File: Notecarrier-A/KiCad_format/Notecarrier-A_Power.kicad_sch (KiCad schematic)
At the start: 42 parts, among them J10 00711, J12 B2B-PH-SM4-TBT(LF)(SN), J19 10118192-0002LF, J19 NU, J3 B2B-PH-SM4-TBT(LF)(SN), J4 B2B-PH-SM4-TBT(LF)(SN), J9 12734, SW1 CJS-1200TA, U2 BQ24210DQCT, U3 MAX17225ELT, U4 TPS62748YFPT

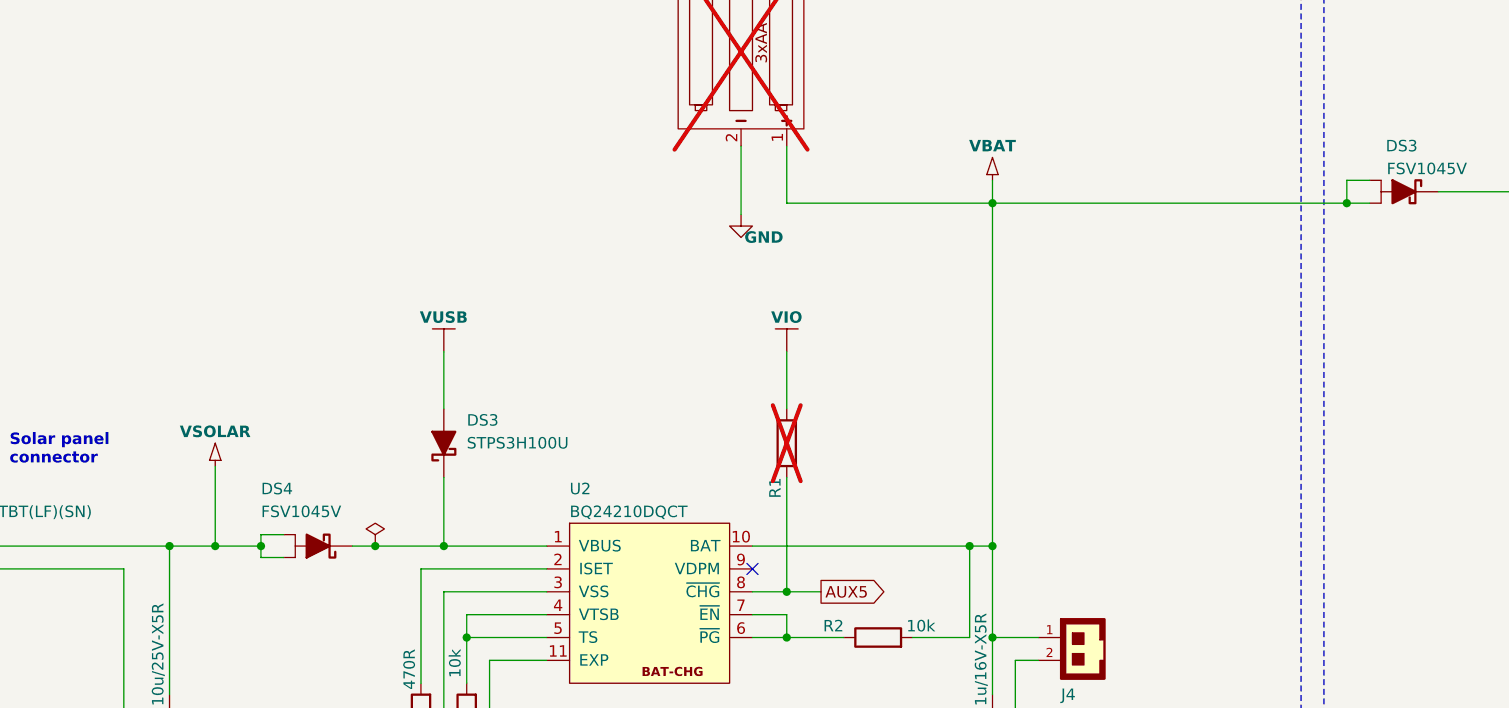
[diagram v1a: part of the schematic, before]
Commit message: First pass port of Notecarrier-B PCB.
See PortingNotes for details. To go: 3D models and validation.
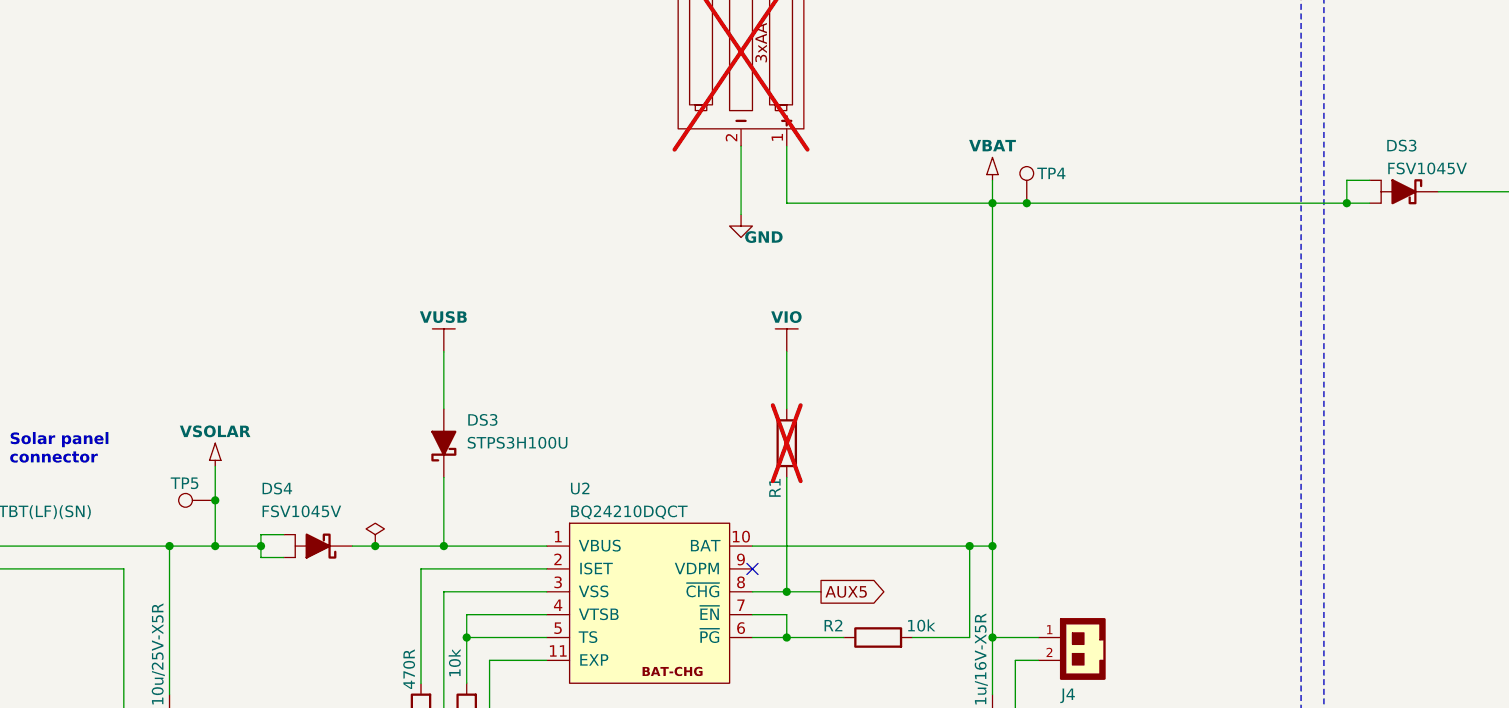
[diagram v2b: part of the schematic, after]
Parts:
- added TP4, TP5: TPS, blues-kicad-lib:TPS-SPEA, symbol Connector:TestPoint
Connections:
- net VBAT: now also TP4.1
- net VSOLAR: now also TP5.1
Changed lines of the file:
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@@
   (junction (at 298.45 205.74) (diameter 0) (color 0 0 0 0)
   )
+  (junction (at 55.88 153.67) (diameter 0) (color 0 0 0 0)
+  )
   (junction (at 293.37 121.92) (diameter 0) (color 0 0 0 0)
   )
@@
   (junction (at 50.8 158.75) (diameter 0) (color 0 0 0 0)
   )
+  (junction (at 146.05 120.65) (diameter 0) (color 0 0 0 0)
+  )
   (junction (at 55.88 158.75) (diameter 0) (color 0 0 0 0)
   )
@@
     (stroke (width 0.6) (type default) (color 0 0 0 1))
   )
+  (wire (pts (xy 50.8 158.75) (xy 55.88 158.75))
+    (stroke (width 0) (type default))
+  )
   (wire (pts (xy 246.38 101.6) (xy 290.83 101.6))
     (stroke (width 0.6) (type default) (color 132 132 132 1))
@@
     (stroke (width 0) (type default))
   )
-  (wire (pts (xy 55.88 158.75) (xy 50.8 158.75))
-    (stroke (width 0) (type default))
-  )
   (wire (pts (xy 290.83 152.4) (xy 290.83 127))
     (stroke (width 0.6) (type default) (color 0 0 0 1))
@@
     (stroke (width 0) (type default))
   )
-  (wire (pts (xy 142.24 120.65) (xy 181.61 120.65))
+  (wire (pts (xy 142.24 120.65) (xy 146.05 120.65))
     (stroke (width 0.6) (type default) (color 255 128 0 1))
   )
@@
     (stroke (width 0.6) (type default) (color 132 132 132 1))
   )
+  (wire (pts (xy 55.88 153.67) (xy 55.88 158.75))
+    (stroke (width 0) (type default))
+  )
   (wire (pts (xy 382.27 121.92) (xy 382.27 139.7))
     (stroke (width 0.6) (type default) (color 255 0 255 1))
@@
     (stroke (width 0) (type default))
   )
-  (wire (pts (xy 55.88 149.86) (xy 55.88 158.75))
+  (wire (pts (xy 55.88 149.86) (xy 55.88 153.67))
     (stroke (width 0) (type default))
   )
@@
     (stroke (width 0) (type default))
   )
+  (wire (pts (xy 146.05 120.65) (xy 181.61 120.65))
+    (stroke (width 0.6) (type default) (color 255 128 0 1))
+  )
   (wire (pts (xy 293.37 121.92) (xy 298.45 121.92))
     (stroke (width 0) (type default))
@@
     )
   )
+  (symbol (lib_id "Connector:TestPoint") (at 146.05 120.65 0) (unit 1)
+    (in_bom yes) (on_board yes) (dnp no)
+    (property "Reference" "TP4" (at 147.2208 117.3891 0)
+      (effects (font (size 1.27 1.27)) (justify left))
+    )
+    (property "Value" "TPS" (at 147.32 119.38 0)
+      (effects (font (size 1.27 1.27)) (justify left) hide)
+    )
+    (property "Footprint" "blues-kicad-lib:TPS-SPEA" (at 151.13 120.65 0)
+      (effects (font (size 1.27 1.27)) hide)
+    )
+    (property "Datasheet" "~" (at 151.13 120.65 0)
+      (effects (font (size 1.27 1.27)) hide)
+    )
+    (property "Critical" "" (at 146.05 120.65 0)
+      (effects (font (size 1.27 1.27)) hide)
+    )
+    (property "Description" "" (at 146.05 120.65 0)
+      (effects (font (size 1.27 1.27)) hide)
+    )
+    (property "Manufacturer" "" (at 146.05 120.65 0)
+      (effects (font (size 1.27 1.27)) hide)
+    )
+    (property "Order Code" "" (at 146.05 120.65 0)
+      (effects (font (size 1.27 1.27)) hide)
+    )
+    (property "Part Number" "" (at 146.05 120.65 0)
+      (effects (font (size 1.27 1.27)) hide)
+    )
+    (property "Supplier" "" (at 146.05 120.65 0)
+      (effects (font (size 1.27 1.27)) hide)
+    )
+    (pin "1")
+    (instances
+      (project "Notecarrier-A"
+        (path "/5050c972-9893-4dc9-ac8b-afa1eb9e3ab8/03718417-b36a-4e5d-916f-df242c9477be"
+          (reference "TP4") (unit 1)
+        )
+      )
+    )
+  )
   (symbol (lib_id "Connector_Generic:Conn_01x03") (at 292.1 205.74 0) (mirror y) (unit 1)
     (in_bom yes) (on_board yes) (dnp no)
@@
         )
       )
+    )
+  )
+  (symbol (lib_id "Connector:TestPoint") (at 55.88 153.67 90) (unit 1)
+    (in_bom yes) (on_board yes) (dnp no)
+    (property "Reference" "TP5" (at 54.1541 151.8113 90)
+      (effects (font (size 1.27 1.27)) (justify left))
+    )
+    (property "Value" "TPS" (at 53.34 156.21 90)
+      (effects (font (size 1.27 1.27)) (justify left) hide)
+    )
+    (property "Footprint" "blues-kicad-lib:TPS-SPEA" (at 55.88 148.59 0)
+      (effects (font (size 1.27 1.27)) hide)
+    )
+    (property "Datasheet" "~" (at 55.88 148.59 0)
+      (effects (font (size 1.27 1.27)) hide)
+    )
+    (property "Critical" "" (at 55.88 153.67 0)
+      (effects (font (size 1.27 1.27)) hide)
+    )
+    (property "Description" "" (at 55.88 153.67 0)
+      (effects (font (size 1.27 1.27)) hide)
+    )
+    (property "Manufacturer" "" (at 55.88 153.67 0)
+      (effects (font (size 1.27 1.27)) hide)
+    )
+    (property "Order Code" "" (at 55.88 153.67 0)
+      (effects (font (size 1.27 1.27)) hide)
+    )
+    (property "Part Number" "" (at 55.88 153.67 0)
+      (effects (font (size 1.27 1.27)) hide)
+    )
+    (property "Supplier" "" (at 55.88 153.67 0)
+      (effects (font (size 1.27 1.27)) hide)
+    )
+    (pin "1")
+    (instances
+      (project "Notecarrier-A"
+        (path "/5050c972-9893-4dc9-ac8b-afa1eb9e3ab8/03718417-b36a-4e5d-916f-df242c9477be"
+          (reference "TP5") (unit 1)
+        )
+      )

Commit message: Release RevA of Notecarrier-A port.
Validation complete. Results in the validation directory, documented in PortingNotes.md.
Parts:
- R1: value 10k -> NU
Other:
- note added: "Additional Interfaces"
- moved on the sheet: C1, J10, J12, J3, PAD1, PAD2, TP5

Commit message: Back port J-5-0065-FOS-USB10118192-NOF footprint from Notecarrier-Pi.
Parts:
- J19: footprint blues-kicad-lib:J-5-0065-FOS-MICROUSB10118192 -> blues-kicad-lib:J-5-0065-FOS-USB10118192-NOF
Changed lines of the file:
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@@
       (effects (font (size 1.27 1.27)) (justify left) hide)
     )
-    (property "Footprint" "blues-kicad-lib:J-5-0065-FOS-MICROUSB10118192" (at 128.27 260.35 0)
+    (property "Footprint" "blues-kicad-lib:J-5-0065-FOS-USB10118192-NOF" (at 128.27 260.35 0)
       (effects (font (size 1.27 1.27)) hide)
     )
@@
       (effects (font (size 1.27 1.27)) hide)
     )
+    (property "Critical" "" (at 124.46 259.08 0)
+      (effects (font (size 1.27 1.27)) hide)
+    )
+    (property "Manufacturer" "" (at 124.46 259.08 0)
+      (effects (font (size 1.27 1.27)) hide)
+    )
+    (property "Order Code" "" (at 124.46 259.08 0)
+      (effects (font (size 1.27 1.27)) hide)
+    )
+    (property "Part Number" "" (at 124.46 259.08 0)
+      (effects (font (size 1.27 1.27)) hide)
+    )
+    (property "Supplier" "" (at 124.46 259.08 0)
+      (effects (font (size 1.27 1.27)) hide)
+    )
